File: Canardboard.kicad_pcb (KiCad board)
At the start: 4 copper layers, 50 x 58.8 mm, 149 parts, among them IC1 SIC437DED-T1-GE3, J1 RBUS, J2 USB_C_Receptacle_USB2.0, J3 Micro_SD_Card_Det, J4 Conn_01x02_Male, J5 Conn_01x03_Male, J6 Conn_01x03_Male, J7 Conn_01x03_Male, Q1 PXP012-30QLJ, Q2 PXP012-30QLJ, Q4 PXP012-30QLJ, Q6 PXP012-30QLJ, U1 ESP32-S3, U10 MP28167GQ-A-Z, U2 SN65HVD230, U3 LTC4412xS6, U4 LTC4412xS6, U7 ICM-20608-G, U8 MMC5983MA, Y1 40MHz±10ppm

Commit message: weird 3v3 and 3.3v bug
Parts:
- added C20: 1uF, Capacitor_SMD:C_0402_1005Metric, F.Cu at (103.0, 119.8)
- added C22: 1uF, Capacitor_SMD:C_0402_1005Metric, F.Cu at (109.1, 120.0)
- added JP3: SolderJumper_2_Open, Jumper:SolderJumper-2_P1.3mm_Open_RoundedPad1.0x1.5mm, F.Cu at (113.7, 102.5)
- added R15: 570, Resistor_SMD:R_0402_1005Metric, F.Cu at (106.2, 118.8)
- added R16: 1.5k, Resistor_SMD:R_0402_1005Metric, F.Cu at (104.8, 119.3)
- added R23: 1.5k, Resistor_SMD:R_0402_1005Metric, F.Cu at (107.7, 119.3)
- added R42: 570, Resistor_SMD:R_0402_1005Metric, F.Cu at (106.2, 116.9)
- added R43: 1.5k, Resistor_SMD:R_0402_1005Metric, F.Cu at (103.8, 121.7)
- added R44: 570, Resistor_SMD:R_0402_1005Metric, F.Cu at (104.8, 121.7)
- added R45: 1.5k, Resistor_SMD:R_0402_1005Metric, F.Cu at (109.0, 121.9)
- added R46: 570, Resistor_SMD:R_0402_1005Metric, F.Cu at (110.2, 120.4)
- added R47: 100k, Resistor_SMD:R_0402_1005Metric, F.Cu at (108.9, 123.8)
- added U5: 74AHC1G00, Package_TO_SOT_SMD:SOT-353_SC-70-5, F.Cu at (104.1, 117.4)
- added U6: 74AHC1G08, Package_TO_SOT_SMD:SOT-353_SC-70-5, F.Cu at (106.9, 121.2)
- moved TP7 148.5 mm to (118.1, 92.3)
- moved R14 16.4 mm to (136.1, 77.0), turned to -90 degrees
- moved C11 12.8 mm to (119.7, 102.3), turned to 180 degrees
- moved D4 6.94 mm to (109.6, 127.6), turned to -90 degrees
- moved TP14 5.58 mm to (117.9, 105.1)
- moved TP15 5.26 mm to (119.7, 105.1)
- moved C16 3.39 mm to (133.6, 122.3)
- moved R8 3.39 mm to (132.1, 121.7)
- moved D1 3.39 mm to (127.6, 124.8)
- moved R9 3.39 mm to (127.2, 121.2)
- moved C15 3.39 mm to (134.7, 122.3)
- moved C17 3.39 mm to (128.4, 127.0)
- moved C18 3.39 mm to (126.6, 122.5)
- moved C19 3.39 mm to (126.5, 127.0)
- moved CANRXLED1 3.39 mm to (136.1, 129.4)
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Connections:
- U3 pad 3: /rbusmosfets/BatteryPower -> Net-(U3-CTL)
- U4 pad 3: GND -> Net-(JP3-A)
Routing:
- net Net-(JP3-A): track 0.00 -> 27.2 mm
- net /servopower/PGOOD: track 9.60 -> 24.5 mm, vias 3 -> 4
- net Net-(U3-CTL): track 0.00 -> 9.30 mm
- net RBUS_uC_V: track 64.8 -> 73.5 mm
- net /rbusmosfets/RBUS_DEPL: track 17.5 -> 25.8 mm
- net GND: track 69.7 -> 74.7 mm, vias 32 -> 44
- net /rbusmosfets/BatteryPower: track 31.9 -> 36.5 mm, vias 0 -> 2
- net /RXD: track 10.8 -> 6.91 mm
- net /SERVO_SGNL1: track 35.6 -> 39.3 mm
- net /SD_DET: track 24.7 -> 28.4 mm
- net /TXD: track 6.17 -> 2.54 mm
- net Net-(R23-Pad1): track 0.00 -> 3.45 mm
- net Net-(R43-Pad2): track 0.00 -> 2.83 mm
- net Net-(R15-Pad1): track 0.00 -> 2.63 mm
- net /SPI_MISO: track 15.8 -> 18.0 mm
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- added copper zone on F.Cu, net +3V3
- added copper zone on F.Cu, net Net-(Q4-S_1)
- added copper zone on F.Cu, net Net-(U10-SW1)
- added copper zone on F.Cu, net Net-(U10-SW2)
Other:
- board size 50 x 58.8 mm -> 49.5 x 58.2 mm

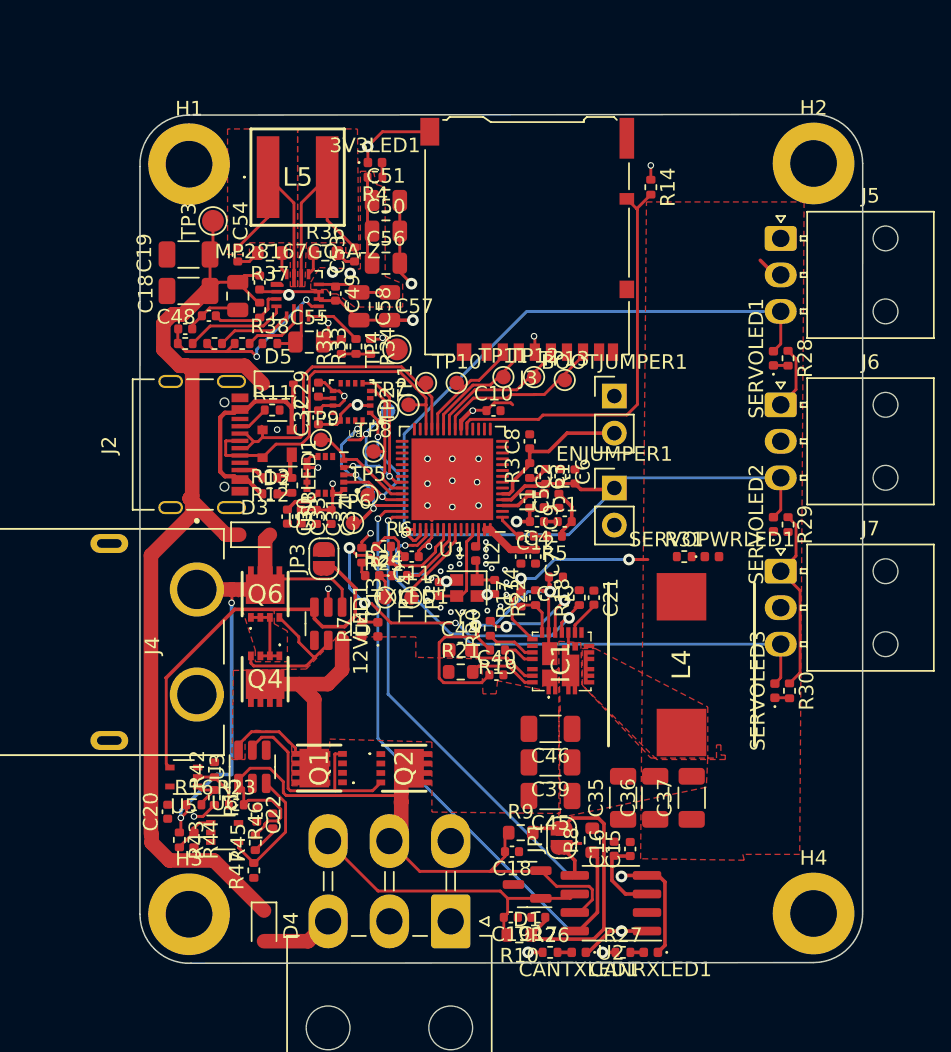
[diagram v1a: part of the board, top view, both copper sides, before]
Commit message: almost all drc fixed (65 left)
- J2 hole intersects with pads? USB
- 3.3 regulator courtyard self intersecting?
- courtyard overlaps (does this matter?)
- padstack not valid? this is testpoints on the back with traces on the back, why is this bad?
- expected SMD actual through hole?
- front solder mask bridges items ?? testpoitns are on back layer
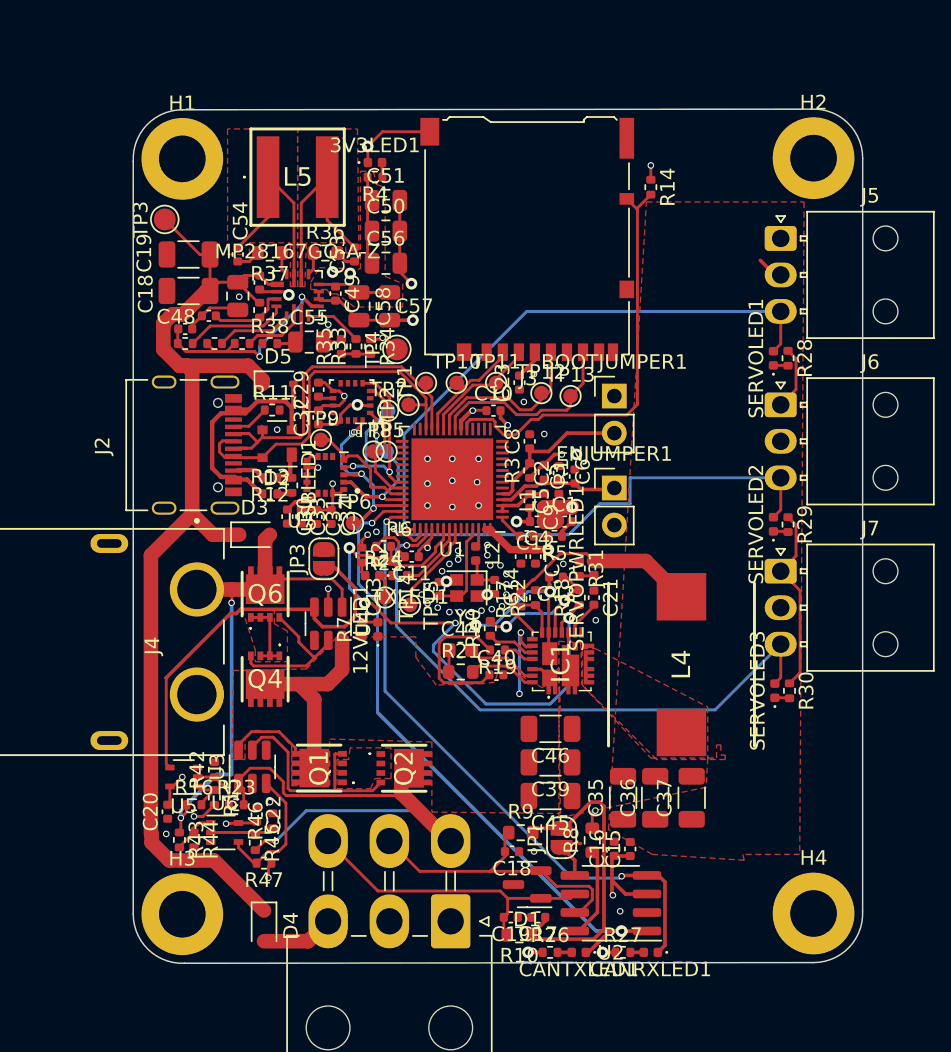
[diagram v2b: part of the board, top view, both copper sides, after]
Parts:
- added C23: 1uF, Capacitor_SMD:C_0402_1005Metric, F.Cu at (127.1, 90.4)
- moved SERVOPWRLED1 8.12 mm to (132.2, 103.1), turned to 90 degrees
- moved R31 7.24 mm to (131.2, 103.1), turned to -90 degrees
- moved TP3 3.30 mm to (102.8, 79.2)
- moved TP5 3.27 mm to (118.0, 95.1)
- moved TP12 1.21 mm to (128.6, 91.1)
- moved TP13 1.17 mm to (130.6, 91.3)
- moved R47 0.86 mm to (109.6, 123.3), turned to 180 degrees
- moved TP11 0.64 mm to (125.5, 90.4)
- moved H1 0.59 mm to (104.0, 75.1)
- moved TP15 0.51 mm to (119.6, 105.6)
- moved H3 0.46 mm to (104.0, 126.8)
- moved J2 0.45 mm to (105.0, 94.7)
- moved H2 0.36 mm to (147.2, 75.0)
- moved R1 0.31 mm to (128.8, 96.5)
- moved C2 0.23 mm to (129.8, 96.6)
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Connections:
- C1 pad 1: +3V3 -> +3.3V
- C10 pad 1: +3V3 -> +3.3V
- C11 pad 1: +3V3 -> +3.3V
- C15 pad 1: +3V3 -> +3.3V
- C16 pad 1: +3V3 -> +3.3V
- C31 pad 1: +3V3 -> +3.3V
- C32 pad 1: +3V3 -> +3.3V
- C33 pad 1: +3V3 -> +3.3V
- C34 pad 1: +3V3 -> +3.3V
- C4 pad 1: +3V3 -> +3.3V
- C49 pad 1: +3V3 -> +3.3V
- C5 pad 1: +3V3 -> +3.3V
- C50 pad 1: +3V3 -> +3.3V
- C51 pad 1: +3V3 -> +3.3V
- C56 pad 1: +3V3 -> +3.3V
- C57 pad 1: +3V3 -> +3.3V
- C58 pad 1: +3V3 -> +3.3V
- C7 pad 1: +3V3 -> +3.3V
- C9 pad 1: +3V3 -> +3.3V
- J3 pad 4: +3V3 -> +3.3V
- L1 pad 1: +3V3 -> +3.3V
- R1 pad 1: +3V3 -> +3.3V
- R14 pad 1: +3V3 -> +3.3V
- R2 pad 1: +3V3 -> +3.3V
- R26 pad 1: +3V3 -> +3.3V
- R27 pad 1: +3V3 -> +3.3V
- R3 pad 1: +3V3 -> +3.3V
- R34 pad 1: +3V3 -> +3.3V
- R4 pad 2: +3V3 -> +3.3V
- TP4 pad 1: +3V3 -> +3.3V
- U1 pad 20: +3V3 -> +3.3V
- U1 pad 46: +3V3 -> +3.3V
- U1 pad 55: +3V3 -> +3.3V
- U1 pad 56: +3V3 -> +3.3V
- U10 pad 12: +3V3 -> +3.3V
- U2 pad 3: +3V3 -> +3.3V
- U7 pad 1: +3V3 -> +3.3V
- U7 pad 16: +3V3 -> +3.3V
- U8 pad 13: +3V3 -> +3.3V
- U8 pad 2: +3V3 -> +3.3V
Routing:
- net +3.3V: track 0.13 -> 60.4 mm, vias 0 -> 19
- net +3V3: track 48.7 -> 0.00 mm, vias 12 -> 0
- net /rbusmosfets/RBUS_DEPL: track 25.8 -> 37.1 mm, vias 0 -> 1
- net /servopower/PGOOD: track 24.5 -> 34.6 mm
- net +12V: track 19.4 -> 26.8 mm, vias 0 -> 2
- net /SERVO_SGNL3: track 36.0 -> 41.6 mm
- net /CAN_TX: track 40.5 -> 44.4 mm
- net /CAN_RX: track 39.0 -> 42.6 mm
- net /SERVO_PWR: track 15.6 -> 18.8 mm, vias 2 -> 0
- net /servopower/VDD: track 8.48 -> 11.3 mm
- net /SERVO_SGNL2: track 32.2 -> 35.0 mm
- net GND: track 74.7 -> 72.2 mm, vias 44 -> 56
- net Net-(R45-Pad1): track 2.00 -> 4.37 mm
- net RBUS_uC_V: track 73.5 -> 75.7 mm
- net /SD_MISO: track 11.6 -> 13.8 mm
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- added copper zone on F.Cu, net +3.3V
- added copper zone on In2.Cu, net +3.3V
- added copper zone on F.Cu, net Net-(Q1-S_1)
- removed copper zone on F.Cu, net +3V3
- removed copper zone on In2.Cu, net +3V3
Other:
- board size 49.5 x 58.2 mm -> 50 x 58.5 mm

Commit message: everything should be fine
fixed all mask stuff
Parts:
- TP5, TP7: moved to B.Cu
- moved TP7 0.06 mm to (118.0, 92.3), turned to 180 degrees
- turned TP5 to 180 degrees
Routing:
- added copper zone on B.Cu, net GND
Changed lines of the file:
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@@
     )
   )
-  (footprint "TestPoint:TestPoint_Pad_D1.0mm" (layer "F.Cu")
-    (at 118 95.1)
-    (descr "SMD pad as test Point, diameter 1.0mm")
-    (tags "test point SMD pad")
-    (property "Sheetfile" "comps.kicad_sch")
-    (property "Sheetname" "comps")
-    (property "ki_description" "test point")
-    (property "ki_keywords" "test point tp")
-    (attr exclude_from_pos_files)
-    (fp_text reference "TP5" (at 0 -1.448) (layer "F.SilkS")
-        (effects (font (size 1 1) (thickness 0.15)))
-    )
-    (fp_text value "TestPoint" (at 0 1.55) (layer "F.Fab")
-        (effects (font (size 1 1) (thickness 0.15)))
-    )
-    (fp_text user "${REFERENCE}" (at 0 -1.45) (layer "F.Fab")
-        (effects (font (size 1 1) (thickness 0.15)))
-    )
-    (fp_circle (center 0 0) (end 0 0.7)
-      (stroke (width 0.12) (type solid)) (fill none) (layer "F.SilkS"))
-    (fp_circle (center 0 0) (end 1 0)
-      (stroke (width 0.05) (type solid)) (fill none) (layer "F.CrtYd"))
-    (pad "1" smd circle (at 0 0) (size 1 1) (layers "B.Cu" "F.Mask")
-      (net 54 "/SPI_CLK") (pinfunction "1") (pintype "passive"))
-  )
   (footprint "TestPoint:TestPoint_Pad_D1.5mm" (layer "F.Cu")
     (at 102.8 79.2 90)
@@
     )
   )
-  (footprint "TestPoint:TestPoint_Pad_D1.0mm" (layer "F.Cu")
-    (at 118.1 92.3)
-    (descr "SMD pad as test Point, diameter 1.0mm")
-    (tags "test point SMD pad")
-    (property "Sheetfile" "comps.kicad_sch")
-    (property "Sheetname" "comps")
-    (property "ki_description" "test point")
-    (property "ki_keywords" "test point tp")
-    (attr exclude_from_pos_files)
-    (fp_text reference "TP7" (at 0 -1.448) (layer "F.SilkS")
-        (effects (font (size 1 1) (thickness 0.15)))
-    )
-    (fp_text value "TestPoint" (at 0 1.55) (layer "F.Fab")
-        (effects (font (size 1 1) (thickness 0.15)))
-    )
-    (fp_text user "${REFERENCE}" (at 0 -1.45) (layer "F.Fab")
-        (effects (font (size 1 1) (thickness 0.15)))
-    )
-    (fp_circle (center 0 0) (end 0 0.7)
-      (stroke (width 0.12) (type solid)) (fill none) (layer "F.SilkS"))
-    (fp_circle (center 0 0) (end 1 0)
-      (stroke (width 0.05) (type solid)) (fill none) (layer "F.CrtYd"))
-    (pad "1" smd circle (at 0 0) (size 1 1) (layers "B.Cu" "F.Mask")
-      (net 55 "/SPI_MISO") (pinfunction "1") (pintype "passive"))
-  )
   (footprint "Capacitor_SMD:C_0402_1005Metric" (layer "F.Cu")
     (at 128.2 102.3 -90)
@@
     )
   )
+  (footprint "TestPoint:TestPoint_Pad_D1.0mm" (layer "B.Cu")
+    (at 118 95.1 180)
+    (descr "SMD pad as test Point, diameter 1.0mm")
+    (tags "test point SMD pad")
+    (property "Sheetfile" "comps.kicad_sch")
+    (property "Sheetname" "comps")
+    (property "ki_description" "test point")
+    (property "ki_keywords" "test point tp")
+    (attr exclude_from_pos_files)
+    (fp_text reference "TP5" (at 0 1.448) (layer "B.SilkS")
+        (effects (font (size 1 1) (thickness 0.15)) (justify mirror))
+    )
+    (fp_text value "TestPoint" (at 0 -1.55) (layer "B.Fab")
+        (effects (font (size 1 1) (thickness 0.15)) (justify mirror))
+    )
+    (fp_text user "${REFERENCE}" (at 0 1.45) (layer "B.Fab")
+        (effects (font (size 1 1) (thickness 0.15)) (justify mirror))
+    )
+    (fp_circle (center 0 0) (end 0 -0.7)
+      (stroke (width 0.12) (type solid)) (fill none) (layer "B.SilkS"))
+    (fp_circle (center 0 0) (end 1 0)
+      (stroke (width 0.05) (type solid)) (fill none) (layer "B.CrtYd"))
+    (pad "1" smd circle (at 0 0 180) (size 1 1) (layers "B.Cu" "B.Mask")
+      (net 54 "/SPI_CLK") (pinfunction "1") (pintype "passive"))
+  )
+  (footprint "TestPoint:TestPoint_Pad_D1.0mm" (layer "B.Cu")
+    (at 118.05 92.325 180)
+    (descr "SMD pad as test Point, diameter 1.0mm")
+    (tags "test point SMD pad")
+    (property "Sheetfile" "comps.kicad_sch")
+    (property "Sheetname" "comps")
+    (property "ki_description" "test point")
+    (property "ki_keywords" "test point tp")
+    (attr exclude_from_pos_files)
+    (fp_text reference "TP7" (at 0 1.448) (layer "B.SilkS")
+        (effects (font (size 1 1) (thickness 0.15)) (justify mirror))
+    )
+    (fp_text value "TestPoint" (at 0 -1.55) (layer "B.Fab")
+        (effects (font (size 1 1) (thickness 0.15)) (justify mirror))
+    )
+    (fp_text user "${REFERENCE}" (at 0 1.45) (layer "B.Fab")
+        (effects (font (size 1 1) (thickness 0.15)) (justify mirror))
+    )
+    (fp_circle (center 0 0) (end 0 -0.7)
+      (stroke (width 0.12) (type solid)) (fill none) (layer "B.SilkS"))
+    (fp_circle (center 0 0) (end 1 0)
+      (stroke (width 0.05) (type solid)) (fill none) (layer "B.CrtYd"))
+    (pad "1" smd circle (at 0 0 180) (size 1 1) (layers "B.Cu" "B.Mask")
+      (net 55 "/SPI_MISO") (pinfunction "1") (pintype "passive"))
+  )
   (gr_line (start 150.609209 126.58204) (end 150.613406 75.000007)
     (stroke (width 0.1) (type default)) (layer "Edge.Cuts"))
@@
   (zone (net 37) (net_name "/servopower/SW") (layer "F.Cu") (hatch edge 0.5)
     (priority 4)
-    (connect_pads (clearance 0))
+    (connect_pads yes (clearance 0))
     (min_thickness 0.25) (filled_areas_thickness no)
     (fill yes (thermal_gap 0.5) (thermal_bridge_width 0.5))
@@
         (xy 140 112.6)
         (xy 140 116.1)
-        (xy 140.6 116.1)
-        (xy 140.6 115.2)
-        (xy 140.9 115.2)
-        (xy 140.9 115.9)
-        (xy 141.2 115.9)
-        (xy 141.2 116.2)
         (xy 136.5 116.2)
         (xy 131.4 111.1)
@@
     )
   )
-  (zone (net 1) (net_name "GND") (layer "F.Cu") (hatch edge 0.5)
-    (connect_pads yes (clearance 0))
-    (min_thickness 0.25) (filled_areas_thickness no)
-    (fill yes (thermal_gap 0.5) (thermal_bridge_width 0.5))
-    (polygon
-      (pts
-        (xy 55.5 50.3)
-        (xy 48.7 169.9)
-        (xy 177.9 172.7)
-        (xy 186.8 51.3)
-      )
-    )
-  )
   (zone (net 130) (net_name "+3.3V") (layer "F.Cu") (hatch edge 0.5)
     (priority 9)
@@
       )
     )
+  )
+  (zone (net 1) (net_name "GND") (layers "F&B.Cu") (hatch edge 0.5)
+    (connect_pads yes (clearance 0))
+    (min_thickness 0.25) (filled_areas_thickness no)
+    (fill yes (thermal_gap 0.5) (thermal_bridge_width 0.5))
+    (polygon
+      (pts
+        (xy 55.5 50.3)
+        (xy 48.7 169.9)
+        (xy 177.9 172.7)
+        (xy 186.8 51.3)
+      )
+    )

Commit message: fixed all of andrei's comments v1
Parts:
- removed the C18 at (126.6, 122.5)
- removed the C19 at (126.5, 127.0)
- removed JP3: SolderJumper_2_Open, Jumper:SolderJumper-2_P1.3mm_Open_RoundedPad1.0x1.5mm
- added C24: DNP, Capacitor_SMD:C_0402_1005Metric, B.Cu at (114.9, 76.4)
- added C25: DNP, Capacitor_SMD:C_0402_1005Metric, B.Cu at (119.6, 83.4)
- added C26: 0.1uF, Capacitor_SMD:C_0402_1005Metric, B.Cu at (116.8, 86.5)
- added JP2: TermJP, Jumper:SolderJumper-2_P1.3mm_Open_RoundedPad1.0x1.5mm, F.Cu at (117.8, 74.9)
- added R48: 100k, Resistor_SMD:R_0402_1005Metric, F.Cu at (114.0, 102.5)
- added R49: 0, Resistor_SMD:R_0402_1005Metric, F.Cu at (112.8, 102.5)
- added R50: DNP, Resistor_SMD:R_0402_1005Metric, B.Cu at (116.3, 84.9)
- added R51: DNP, Resistor_SMD:R_0402_1005Metric, B.Cu at (115.8, 86.5)
- added U9: SC4215, iclr:SOIC127P599X175-9N, B.Cu at (116.2, 80.6)
- C44: footprint Capacitor_SMD:C_0603_1608Metric -> Capacitor_SMD:C_0402_1005Metric
- C55: footprint Capacitor_SMD:C_0805_2012Metric -> Capacitor_SMD:C_0402_1005Metric
- R15, R42, R44, R46: value 570 -> 470
- R16, R23, R43, R45: value 1.5k -> 1k
- R21, R36, R37, R8: footprint Resistor_SMD:R_0603_1608Metric -> Resistor_SMD:R_0402_1005Metric
- U1: footprint Package_DFN_QFN:QFN-56-1EP_7x7mm_P0.4mm_EP5.6x5.6mm -> iclr:QFN40P700X700X90-57N
- moved C35 12.9 mm to (146.1, 113.6), turned to 0 degrees
- moved C52 10.8 mm to (114.9, 85.7)
- moved C36 10.1 mm to (146.1, 116.1), turned to 0 degrees
- moved R26 9.16 mm to (138.4, 129.5), turned to 180 degrees
- moved R8 7.76 mm to (132.8, 129.5), turned to 0 degrees
- moved R27 7.62 mm to (138.3, 123.0), turned to 180 degrees
- moved R9 7.49 mm to (127.9, 128.7)
- moved C37 7.18 mm to (146.1, 118.6), turned to 0 degrees
- moved C16 7.12 mm to (140.4, 124.4), turned to 0 degrees
- moved C15 6.52 mm to (140.4, 125.5), turned to 0 degrees
- moved CANRXLED1 6.41 mm to (136.4, 123.0), turned to 0 degrees
- moved L4 6.16 mm to (138.5, 115.8)
- moved CANTXLED1 5.23 mm to (136.4, 129.5), turned to 0 degrees
- moved R10 4.62 mm to (127.9, 123.7)
- moved R4 3.51 mm to (118.7, 73.2), turned to 0 degrees
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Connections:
- C49 pad 1: +3.3V -> /servopower/uC_VOUT
- C50 pad 1: +3.3V -> /servopower/uC_VOUT
- C51 pad 1: +3.3V -> /servopower/uC_VOUT
- C56 pad 1: +3.3V -> /servopower/uC_VOUT
- C57 pad 1: +3.3V -> /servopower/uC_VOUT
- C58 pad 1: +3.3V -> /servopower/uC_VOUT
- IC1 pad 19: +12V -> /SERVOBUCK_EN
- R34 pad 1: +3.3V -> /servopower/uC_VOUT
- U1 pad 14: unconnected-(U1-GPIO9/ADC1_CH8-Pad14) -> /SERVOBUCK_EN
- U10 pad 12: +3.3V -> /servopower/uC_VOUT
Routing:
- net /SERVOBUCK_EN: track 0.00 -> 47.4 mm, vias 0 -> 2
- net GND: track 72.2 -> 54.8 mm, vias 56 -> 69
- net Net-(JP1-B): track 21.2 -> 7.11 mm
- net +3.3V: track 60.4 -> 49.6 mm, vias 19 -> 23
- net /SERVO_PWR: track 18.8 -> 11.8 mm
- net +12V: track 26.8 -> 20.8 mm, vias 2 -> 0
- net /CAN-: track 21.4 -> 26.8 mm, vias 0 -> 2
- net /rbusmosfets/RBUS_DEPL: track 37.1 -> 32.4 mm
- net Net-(U2-Rs): track 6.34 -> 1.69 mm
- net /CAN_RX: track 42.6 -> 38.4 mm
- net /servopower/uC_VOUT: track 0.00 -> 3.51 mm, vias 0 -> 2
- net Net-(U9-ADJ): track 0.00 -> 3.05 mm
- net /Data-: track 24.1 -> 25.6 mm
- net RBUS_uC_V: track 75.7 -> 74.2 mm
- net Net-(U4-CTL): track 27.2 -> 28.3 mm
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- added copper zone on B.Cu, net +3.3V
- added copper zone on F.Cu, net /rbusmosfets/BatteryPower
- added copper zone on F.Cu, net /rbusmosfets/RBUS_DEPL
- added copper zone on B.Cu, net /servopower/uC_VOUT
- added copper zone on F.Cu, net /servopower/uC_VOUT
- added copper zone on F.Cu, net RBUS_uC_V
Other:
- board size 50 x 58.5 mm -> 50.7 x 58.7 mm

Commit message: roddy changes
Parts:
- moved R36 0.56 mm to (114.1, 82.0)
- moved R37 0.52 mm to (109.7, 82.0)
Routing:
- net +3.3V: track 49.6 -> 48.0 mm
- net GND: vias 69 -> 71

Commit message: did some stuffus
added a new power plane in servo power on the back side
made SW larger
and a lot more changes
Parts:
- moved C37 16.9 mm to (135.6, 105.4), turned to 180 degrees
- moved C35 14.9 mm to (135.6, 103.0), turned to 180 degrees
- moved C36 13.4 mm to (135.6, 107.8), turned to 180 degrees
- moved H2 5.00 mm to (143.0, 75.0)
- moved H4 5.00 mm to (143.0, 127.0)
- moved J7 4.52 mm to (141.0, 101.2)
- moved J6 4.16 mm to (141.0, 90.8)
- moved J5 4.04 mm to (141.0, 80.3)
- moved SERVOLED3 3.77 mm to (141.9, 108.9), turned to 180 degrees
- moved R30 3.17 mm to (143.8, 108.9), turned to 180 degrees
- moved SERVOLED2 3.13 mm to (141.8, 98.5), turned to 180 degrees
- moved SERVOLED1 2.84 mm to (141.8, 88.0), turned to 180 degrees
- moved C39 2.61 mm to (130.0, 118.9)
- moved C45 2.61 mm to (130.0, 121.2)
- moved C46 2.61 mm to (130.0, 116.6)
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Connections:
- U1 pad 14: /SERVOBUCK_EN -> /SERVO_SGNL2
- U1 pad 44: /SERVO_SGNL2 -> /SERVOBUCK_EN
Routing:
- net /SERVOBUCK_EN: track 47.4 -> 19.8 mm
- net /SERVO_SGNL2: track 35.0 -> 18.6 mm
- net GND: track 54.8 -> 42.3 mm, vias 71 -> 67
- net /SERVO_PWR: track 11.8 -> 16.4 mm, vias 0 -> 5
- net /SERVO_SGNL1: track 39.3 -> 35.2 mm
- net /servopower/PGOOD: track 34.9 -> 31.5 mm
- net /SERVO_SGNL3: track 41.6 -> 38.4 mm
- net /RXD: track 5.91 -> 8.52 mm
- net /servopower/uC_VCC: track 15.1 -> 13.9 mm
- net +3.3V: track 48.0 -> 49.0 mm
- net /Data-: track 25.6 -> 24.9 mm
- added copper zone on B.Cu, net /SERVO_PWR
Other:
- board size 50.7 x 58.7 mm -> 45.7 x 58.7 mm
